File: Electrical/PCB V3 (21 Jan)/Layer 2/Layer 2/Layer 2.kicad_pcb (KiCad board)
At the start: 2 copper layers, 178 x 170 mm, 67 parts, among them Q1 AON6354, Q2 AON6354, Q3 AON6354, Q4 AON6354, SW1 SW_Nidec_CAS-120A1, U2 LM2596S-3.3, U3 VNH5019ATR-E, U4 XT30UPB-M, U5 XT30UPB-M, U6 VNH5019ATR-E, U7 VNH5019ATR-E, U8 VNH5019ATR-E, U9 XT30UPB-M

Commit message: halfway done with motor drivers footprint vias are gay
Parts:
- added L2: L, Connector_PinHeader_2.54mm:PinHeader_1x02_P2.54mm_Vertical_SMD_Pin1Right, F.Cu at (244.8, 61.0)
- added U10: Pinhead1, Connector_PinHeader_2.54mm:PinHeader_1x02_P2.54mm_Vertical_SMD_Pin1Right, F.Cu at (244.8, 68.2)
- added U11: Pinhead 2, Connector_PinHeader_2.54mm:PinHeader_1x02_P2.54mm_Vertical_SMD_Pin1Right, F.Cu at (244.8, 75.3)
- C2, Q1, R1, R2, R3, R4, R5, R6, R7, R8: moved to B.Cu
- U3: footprint layer2v3:IC_VNH5019ATR-E -> layer2v3:fixed -onenew; moved to B.Cu
- U6, U7, U8: footprint layer2v3:IC_VNH5019ATR-E -> layer2v3:fixed -onenew
- moved U9 254.3 mm to (109.4, 73.3)
- moved C2 131.4 mm to (292.3, 165.5), turned to 180 degrees
- moved R3 125.2 mm to (295.1, 151.4)
- moved R1 124.5 mm to (295.1, 144.8)
- moved R4 121.2 mm to (291.1, 147.3), turned to 180 degrees
- moved R2 120.2 mm to (298.8, 144.8), turned to 180 degrees
- moved R5 118.4 mm to (295.0, 149.3), turned to 180 degrees
- moved R7 117.5 mm to (291.1, 151.6), turned to 180 degrees
- moved R6 114.3 mm to (291.1, 144.9), turned to 180 degrees
- moved R8 113.4 mm to (291.0, 149.4), turned to 180 degrees
- moved U3 112.2 mm to (278.5, 150.5), turned to 180 degrees
- moved Q1 67.5 mm to (292.7, 155.8), turned to 90 degrees
- moved SW1 1.79 mm to (376.0, 88.3)
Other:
- outline, holes or cut-outs redrawn

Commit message: yay fixed motor driver do rest mr cos tired djbfj
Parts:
- U3, U6, U7, U8: footprint layer2v3:fixed -onenew -> layer2v3:fixed -onenew-newer

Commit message: cx is annoyingwith 1 drivers
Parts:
- added J1: Conn_01x04, Connector_JST:JST_EH_B4B-EH-A_1x04_P2.50mm_Vertical, B.Cu at (89.1, 76.4)
- added J2: Conn_01x06, Connector_JST:JST_EH_B6B-EH-A_1x06_P2.50mm_Vertical, F.Cu at (91.5, 189.6)
- A1: footprint layer2v3:TEENSY_SHORT -> layer2v3:MODULE_DEV-15583
- C4, Q2, R10, R11, R12, R13, R14, R15, R16, R17, U6: moved to B.Cu
- U10: value Pinhead1 -> XT30UPB-M; footprint Connector_PinHeader_2.54mm:PinHeader_1x02_P2.54mm_Vertical_SMD_Pin1Right -> layer2v3:XT30UPB-M
- U11: value Pinhead 2 -> XT30UPB-M; footprint Connector_PinHeader_2.54mm:PinHeader_1x02_P2.54mm_Vertical_SMD_Pin1Right -> layer2v3:XT30UPB-M
- moved H4 316.3 mm to (27.3, 157.9)
- moved H3 311.9 mm to (27.3, 119.1)
- moved H5 293.3 mm to (78.6, 199.1)
- moved H13 288.4 mm to (86.1, 168.5)
- moved H12 275.0 mm to (84.1, 159.5)
- moved H11 269.4 mm to (84.1, 117.5)
- moved H10 267.2 mm to (86.1, 108.5)
- moved R14 256.7 mm to (115.9, 125.4), turned to 180 degrees
- moved R13 256.3 mm to (116.0, 121.4), turned to 180 degrees
- moved R12 255.5 mm to (118.7, 124.4), turned to 90 degrees
- moved R10 254.8 mm to (119.8, 119.4)
- moved R15 254.1 mm to (115.9, 119.5), turned to 180 degrees
- moved R11 253.9 mm to (120.7, 122.3), turned to 90 degrees
- moved R17 253.7 mm to (115.8, 123.5), turned to 180 degrees
- moved R16 250.5 mm to (120.7, 126.1), turned to -90 degrees
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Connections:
- U3 pad 15: /Motor 2 Out B -> /Motor 1 Out B
- U3 pad 16: /Motor 2 Out B -> /Motor 1 Out B
- U3 pad 21: /Motor 2 Out B -> /Motor 1 Out B
- U3 pad HS3: /Motor 2 Out B -> /Motor 1 Out B
- U4 pad P$1: +5V -> /Motor 1 Out A
- U4 pad P$2: GND -> /Motor 1 Out B
- U5 pad P$1: +3V3 -> /Motor 3 Out A
- U5 pad P$2: GND -> /Motor 3 Out B
- U6 pad 15: /Motor 2 BOut  -> /Motor 2 Out B
- U6 pad 16: /Motor 2 BOut  -> /Motor 2 Out B
- U6 pad 21: /Motor 2 BOut  -> /Motor 2 Out B
- U6 pad HS3: /Motor 2 BOut  -> /Motor 2 Out B
- U8 pad 1: /Motor 4 Motor B -> /Motor 4 Out A
- U8 pad 25: /Motor 4 Motor B -> /Motor 4 Out A
- U8 pad 30: /Motor 4 Motor B -> /Motor 4 Out A
- U8 pad HS2: /Motor 4 Motor B -> /Motor 4 Out A
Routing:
- net /Motor 1 EN A: track 0.00 -> 60.3 mm
- net +3V3: track 0.00 -> 50.3 mm, vias 0 -> 1
- net /Motor 1 EN B: track 0.00 -> 21.0 mm, vias 0 -> 2
- net /Motor 4 Out A: track 0.00 -> 13.3 mm
- net Net-(U3-ENB/DIAGB): track 0.00 -> 8.72 mm
- net Net-(U3-INB): track 0.00 -> 3.10 mm
- net Net-(U3-PWM): track 0.00 -> 2.57 mm
- added copper zone on B.Cu, net +12V
- added copper zone on B.Cu, net +3V3
- added copper zone on B.Cu, net /Motor 1 EN A
- added copper zone on B.Cu, net /Motor 1 Out A
- added copper zone on B.Cu, net /Motor 1 Out B
- added copper zone on B.Cu, net /Motor Driver
- added copper zone on B.Cu, net /PWM Motor 1
- added copper zone on B.Cu, net Net-(C2-Pad1)
- added copper zone on B.Cu, net Net-(Q1-G)
- added copper zone on B.Cu, net Net-(U3-ENA/DIAGA)
- added copper zone on B.Cu, net Net-(U3-INA)

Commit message: motor drivers someone done ish ig this is from yesterday
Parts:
- moved R12 1.91 mm to (118.8, 122.5)
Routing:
- net +3V3: track 50.3 -> 97.7 mm, vias 1 -> 2
- net /Motor Driver: track 0.00 -> 41.0 mm, vias 0 -> 1
- net Net-(U6-INA): track 0.00 -> 2.29 mm
- net /Motor 2 EN A: track 0.00 -> 2.23 mm
- net /Motor 2 EN B: track 0.00 -> 2.16 mm
- net Net-(U6-ENA/DIAGA): track 0.00 -> 2.00 mm
- net Net-(U6-ENB/DIAGB): track 0.00 -> 1.89 mm
- net Net-(U6-PWM): track 0.00 -> 1.89 mm
- added copper zone on B.Cu, net /PWM Motor 2
- added copper zone on B.Cu, net Net-(Q2-G)
- added copper zone on B.Cu, net Net-(U6-INB)

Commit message: last motor driver to be done and jst
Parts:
- removed U9: XT30UPB-M, layer2v3:AMASS_XT60-M
- added J3: XT60-M, layer2v3:AMASS_XT60-M, F.Cu at (109.5, 73.2)
- C6, C8, Q3, Q4, R18, R19, R20, R21, R22, R23, R24, R25, R26, R27, R28, R29, R30, R31, R32, R33, U7, U8: moved to B.Cu
- J2: value Conn_01x06 -> Conn_02x04_Counter_Clockwise; footprint Connector_JST:JST_EH_B6B-EH-A_1x06_P2.50mm_Vertical -> Connector_JST:JST_PHD_B8B-PHDSS_2x04_P2.00mm_Vertical
- moved R30 287.1 mm to (116.1, 176.2), turned to 180 degrees
- moved R29 286.7 mm to (116.1, 172.2), turned to 180 degrees
- moved R28 285.7 mm to (119.9, 174.4)
- moved R32 285.3 mm to (116.2, 178.3), turned to 180 degrees
- moved R31 283.2 mm to (116.1, 170.3), turned to 180 degrees
- moved R33 282.4 mm to (116.1, 174.3), turned to 180 degrees
- moved R27 272.6 mm to (119.9, 178.3)
- moved R22 270.6 mm to (117.7, 154.0), turned to 180 degrees
- moved R21 270.1 mm to (117.7, 150.1), turned to 180 degrees
- moved R26 270.0 mm to (122.8, 175.3), turned to -90 degrees
- moved R24 269.1 mm to (117.7, 156.0), turned to 180 degrees
- moved R20 268.8 mm to (121.4, 152.1)
- moved R19 267.1 mm to (123.0, 148.7), turned to 90 degrees
- moved R23 267.0 mm to (117.9, 148.2), turned to 180 degrees
- moved R25 266.5 mm to (117.6, 152.0), turned to 180 degrees
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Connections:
- A1 pad 10: unconnected-(A1-Pad10) -> /Motor 4 EN A
- A1 pad 11: unconnected-(A1-Pad11) -> /Motor 4 EN B
- A1 pad 12: unconnected-(A1-Pad12) -> /Motor 1 EN A
- A1 pad 13: /Motor 1 EN A -> unconnected-(A1-Pad13)
- A1 pad 14: /Motor 4 EN B -> /TX1
- A1 pad 15: /Motor 4 EN A -> /RX1
- A1 pad 16: /Motor 3 EN B -> /RX2
- A1 pad 17: /Motor 3 EN A -> /TX2
- A1 pad 18: /Motor 2 EN B -> unconnected-(A1-Pad18)
- A1 pad 19: /Motor 2 EN A -> unconnected-(A1-Pad19)
- A1 pad 20: /Motor 1 EN B -> /TX1
- A1 pad 21: unconnected-(A1-Pad21) -> /RX3
- A1 pad 5: unconnected-(A1-Pad5) -> /Motor 1 EN B
- A1 pad 6: unconnected-(A1-Pad6) -> /Motor 2 EN A
- A1 pad 7: unconnected-(A1-Pad7) -> /Motor 2 EN B
- A1 pad 8: unconnected-(A1-Pad8) -> /Motor 3 EN A
- A1 pad 9: unconnected-(A1-Pad9) -> /Motor 3 EN B
- J2 pad 2: /SCL -> /RX1
- J2 pad 3: /SDA -> /TX1
- J2 pad 4: /L3 TX -> /RX2
- J2 pad 5: /L3 RX -> GND
- J2 pad 6: GND -> /TX3
- R26 pad 1: /Motor 4 EN B -> /Motor 4 EN A
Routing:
- net +12V: track 0.00 -> 215.9 mm, vias 0 -> 3
- net /Motor 3 EN A: track 0.00 -> 96.3 mm, vias 0 -> 3
- net /Motor 3 EN B: track 0.00 -> 92.5 mm, vias 0 -> 2
- net /PWM Motor 3: track 0.00 -> 65.4 mm
- net Net-(C4-Pad1): track 0.00 -> 61.5 mm, vias 0 -> 2
- net /Motor Driver: track 41.0 -> 97.7 mm
- net +3V3: track 97.7 -> 147.9 mm
- net Net-(C6-Pad1): track 0.00 -> 37.6 mm
- net Net-(C2-Pad1): track 0.00 -> 16.7 mm, vias 0 -> 2
- net /Motor 4 Out A: track 13.3 -> 0.00 mm
- net /Motor 4 EN A: track 0.00 -> 7.65 mm
- net Net-(U8-INA): track 0.00 -> 3.24 mm
- net Net-(U7-INA): track 0.00 -> 3.08 mm
- net Net-(U7-ENA/DIAGA): track 0.00 -> 2.55 mm
- net Net-(U7-ENB/DIAGB): track 0.00 -> 2.51 mm
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- added copper zone on B.Cu, net /Motor 2 Out A
- added copper zone on B.Cu, net /Motor 2 Out B
- added copper zone on B.Cu, net /Motor 3 Out A
- added copper zone on B.Cu, net /Motor 3 Out B
- added copper zone on B.Cu, net Net-(C4-Pad1)
- added copper zone on B.Cu, net Net-(C6-Pad1)
- added copper zone on B.Cu, net Net-(Q3-G)
- added copper zone on B.Cu, net Net-(Q4-G)
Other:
- board text added: "2-Chairs."

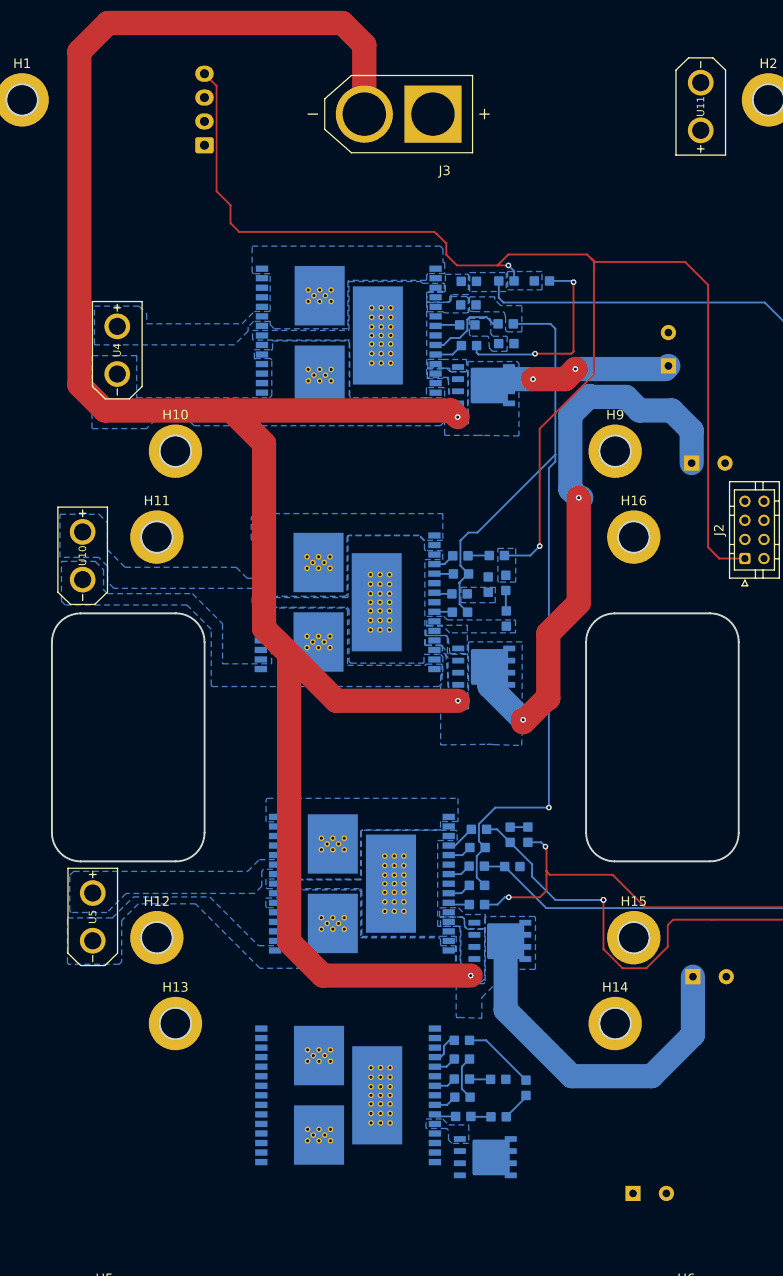
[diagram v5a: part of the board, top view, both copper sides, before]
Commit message: motor drivers r done to be done tmr: diodes footbrint buckies boost capacitors and teensy pwm and motor feedback wiring
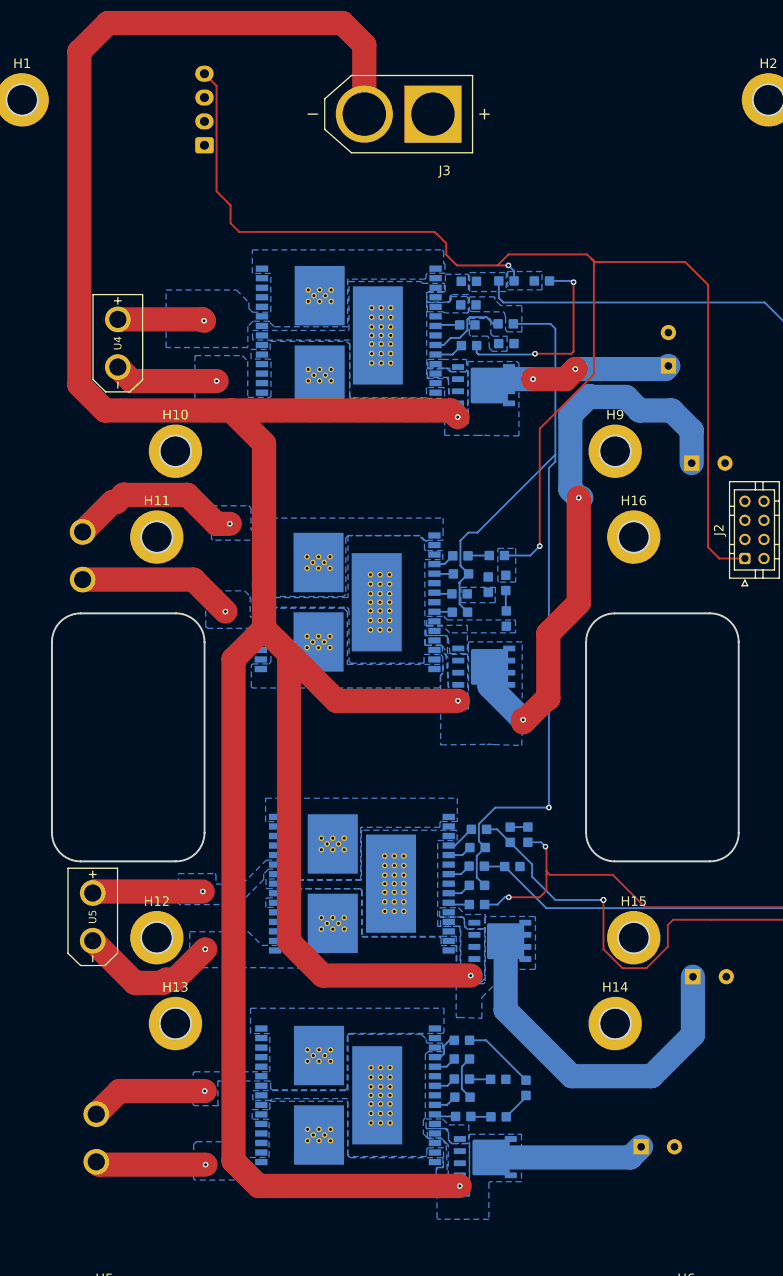
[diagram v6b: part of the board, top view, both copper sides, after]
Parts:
- U10, U11: moved to B.Cu
- moved U11 125.3 mm to (77.8, 180.5), turned to -90 degrees
- moved C8 4.96 mm to (136.6, 181.4)
- moved U4 0.73 mm to (80.0, 97.2)
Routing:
- net +12V: track 215.9 -> 297.8 mm, vias 3 -> 4
- net /Motor 2 Out A: track 0.00 -> 18.3 mm, vias 0 -> 1
- net /Motor 2 Out B: track 0.00 -> 16.4 mm, vias 0 -> 1
- net Net-(C8-Pad1): track 0.00 -> 16.2 mm
- net /Motor 3 Out B: track 0.00 -> 15.1 mm, vias 0 -> 1
- net /Motor 4 Out A: track 0.00 -> 12.4 mm, vias 0 -> 1
- net /Motor 3 Out A: track 0.00 -> 11.6 mm, vias 0 -> 1
- net /Motor 4 Out B: track 0.00 -> 11.6 mm, vias 0 -> 1
- net /Motor 1 Out B: track 0.00 -> 11.0 mm, vias 0 -> 1
- net /Motor 1 Out A: track 0.00 -> 9.10 mm, vias 0 -> 1
- added copper zone on B.Cu, net /Motor 4 Out A
- added copper zone on B.Cu, net /Motor 4 Out B
- added copper zone on B.Cu, net Net-(C8-Pad1)

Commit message: boostie
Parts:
- added C1: 220u, Capacitor_THT:CP_Axial_L10.0mm_D6.0mm_P15.00mm_Horizontal, F.Cu at (245.6, 87.2)
- added C10: 10n, Capacitor_THT:CP_Axial_L10.0mm_D6.0mm_P15.00mm_Horizontal, F.Cu at (260.2, 87.2)
- added C11: 220u, Capacitor_THT:CP_Axial_L10.0mm_D6.0mm_P15.00mm_Horizontal, F.Cu at (260.2, 99.3)
- added C12: 1u, Capacitor_THT:CP_Axial_L10.0mm_D6.0mm_P15.00mm_Horizontal, F.Cu at (131.8, 205.4)
- added C13: 0u1, Capacitor_THT:CP_Axial_L10.0mm_D6.0mm_P15.00mm_Horizontal, F.Cu at (148.7, 186.9)
- added C14: 220uF, Capacitor_THT:CP_Axial_L10.0mm_D6.0mm_P15.00mm_Horizontal, F.Cu at (148.1, 183.5)
- added C3: 220u, Capacitor_THT:CP_Axial_L10.0mm_D6.0mm_P15.00mm_Horizontal, F.Cu at (245.6, 99.3)
- added C5: 0u1, Capacitor_THT:CP_Axial_L10.0mm_D6.0mm_P15.00mm_Horizontal, F.Cu at (108.2, 190.6)
- added C7: 100u, Capacitor_THT:CP_Axial_L10.0mm_D6.0mm_P15.00mm_Horizontal, F.Cu at (104.2, 197.6)
- added C9: 10u, Capacitor_THT:CP_Axial_L10.0mm_D6.0mm_P15.00mm_Horizontal, F.Cu at (245.6, 135.4)
- added D1: SS54, Diode_SMD:D_0201_0603Metric, F.Cu at (282.5, 106.0)
- added D2: SS54, Diode_SMD:D_0201_0603Metric, F.Cu at (282.5, 107.7)
- added D3: SS510, Diode_SMD:D_0201_0603Metric, F.Cu at (132.6, 189.7)
- added L1: 15uH, Inductor_SMD:L_0201_0603Metric, F.Cu at (285.0, 106.0)
- added L3: 68uH, Inductor_SMD:L_APV_APH1040, F.Cu at (115.7, 194.8)
- added R34: 10K, Sen Robo:res0603, F.Cu at (269.7, 106.5)
- added R35: 3K24, Sen Robo:res0603, F.Cu at (269.7, 109.4)
- added R36: 2k94, Sen Robo:res0603, F.Cu at (130.6, 194.4)
- added R37: 57K, Sen Robo:res0603, F.Cu at (132.5, 192.5)
- added R38: 1K5, Sen Robo:res0603, F.Cu at (189.0, 199.5)
- added U1: XT30UPB-M, layer2v3:XT30UPB-M, F.Cu at (137.7, 189.8)
- added U12: TPS5430DDAG4, layer2v3:VREG_TPS79625KTTR, F.Cu at (281.3, 87.3)
- added U9: LM2587S-ADJ, layer2v3:VREG_LM5017MR_NOPB, F.Cu at (125.0, 192.4)
- C2, C4, C6, C8: footprint Sen Robo:CP_Radial_D8.0mm_P3.50mm -> Capacitor_THT:CP_Axial_L10.0mm_D6.0mm_P15.00mm_Horizontal
- moved C8 11.2 mm to (125.5, 182.1)
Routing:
- net +12V: track 297.8 -> 326.1 mm
- net Net-(D3-A): track 0.00 -> 25.3 mm, vias 0 -> 2
- net Net-(C8-Pad1): track 16.2 -> 6.50 mm
- added copper zone on B.Cu, net +24V
- added copper zone on B.Cu, net Net-(D3-A)
- added copper zone on B.Cu, net Net-(U9-COMP)
- added copper zone on B.Cu, net Net-(U9-FB)

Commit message: i think i  added the solenoid boost in this idk
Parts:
- moved R38 55.0 mm to (134.2, 194.3), turned to 0 degrees
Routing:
- added copper zone on B.Cu, net Net-(C12-Pad1)
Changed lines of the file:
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@@
 	(footprint "Sen Robo:res0603"
 		(layer "F.Cu")
-		(at 189.024377 199.51432 90)
+		(at 134.249377 194.31432)
 		(property "Reference" "R38"
-			(at 0 -1.6 90)
+			(at 0 -1.6 360)
 			(layer "F.SilkS")
 			(effects
@@
 		)
 		(property "Value" "1K5"
-			(at 0 1.8 90)
+			(at 0 1.8 0)
 			(unlocked yes)
 			(layer "F.Fab")
@@
 		)
 		(property "Footprint" "Sen Robo:res0603"
-			(at 0 0 90)
+			(at 0 0 360)
 			(layer "F.Fab")
 			(hide yes)
@@
 		)
 		(property "Datasheet" ""
-			(at 0 0 90)
+			(at 0 0 360)
 			(layer "F.Fab")
 			(hide yes)
@@
 		)
 		(property "Description" ""
-			(at 0 0 90)
+			(at 0 0 360)
 			(layer "F.Fab")
 			(hide yes)
@@
 		)
 		(property "LCSC" "C22843"
-			(at 0 0 90)
+			(at 0 0 0)
 			(unlocked yes)
 			(layer "F.Fab")
@@
 		(attr smd)
 		(fp_line
-			(start -1.5 -0.9)
-			(end 1.5 -0.9)
+			(start -1.8 0.6)
+			(end -1.8 -0.6)
 			(stroke
 				(width 0.1)
@@
 		)
 		(fp_line
-			(start 1.8 -0.6)
-			(end 1.8 0.6)
+			(start -1.5 -0.9)
+			(end 1.5 -0.9)
 			(stroke
 				(width 0.1)
@@
 		)
 		(fp_line
-			(start -1.8 0.6)
-			(end -1.8 -0.6)
+			(start -1.5 0.9)
+			(end 1.5 0.9)
 			(stroke
 				(width 0.1)
@@
 		)
 		(fp_line
-			(start -1.5 0.9)
-			(end 1.5 0.9)
+			(start 1.8 -0.6)
+			(end 1.8 0.6)
 			(stroke
 				(width 0.1)
@@
 		)
 		(fp_arc
-			(start 1.5 -0.9)
-			(mid 1.712132 -0.812132)
-			(end 1.8 -0.6)
+			(start -1.8 -0.6)
+			(mid -1.712132 -0.812132)
+			(end -1.5 -0.9)
 			(stroke
 				(width 0.1)
@@
 		)
 		(fp_arc
-			(start -1.8 -0.6)
-			(mid -1.712132 -0.812132)
-			(end -1.5 -0.9)
+			(start -1.5 0.9)
+			(mid -1.712132 0.812132)
+			(end -1.8 0.6)
 			(stroke
 				(width 0.1)
@@
 		)
 		(fp_arc
-			(start 1.8 0.6)
-			(mid 1.712132 0.812132)
-			(end 1.5 0.9)
+			(start 1.5 -0.9)
+			(mid 1.712132 -0.812132)
+			(end 1.8 -0.6)
 			(stroke
 				(width 0.1)
@@
 		)
 		(fp_arc
-			(start -1.5 0.9)
-			(mid -1.712132 0.812132)
-			(end -1.8 0.6)
+			(start 1.8 0.6)
+			(mid 1.712132 0.812132)
+			(end 1.5 0.9)
 			(stroke
 				(width 0.1)
@@
 		)
 		(pad "1" smd roundrect
-			(at -0.8 0 90)
+			(at -0.8 0)
 			(size 1 1)
 			(layers "F.Cu" "F.Paste" "F.Mask")
@@
 		)
 		(pad "2" smd roundrect
-			(at 0.8 0 90)
+			(at 0.8 0)
 			(size 1 1)
 			(layers "F.Cu" "F.Paste" "F.Mask")
@@
 			(pts
 				(xy 150.419377 188.70432) (xy 150.379377 188.74432) (xy 145.479377 188.74432) (xy 145.269377 188.95432)
-				(xy 145.269377 194.24432) (xy 144.059377 195.45432) (xy 132.869377 195.45432) (xy 132.539377 195.12432)
+				(xy 145.269377 193.20432) (xy 145.279377 193.12432) (xy 132.549377 193.12432) (xy 132.539377 193.11432)
 				(xy 132.539377 188.15432) (xy 132.829377 187.86432) (xy 137.359377 187.86432) (xy 137.549377 188.05432)
 				(xy 137.549377 191.64432) (xy 137.739377 191.83432) (xy 142.969377 191.83432) (xy 143.619377 191.18432)
@@
 	)
 	(zone
+		(net 86)
+		(net_name "Net-(C12-Pad1)")
+		(layer "B.Cu")
+		(hatch edge 0.5)
+		(priority 34)
+		(connect_pads yes
+			(clearance 0.2)
+		)
+		(min_thickness 0.25)
+		(filled_areas_thickness no)
+		(fill yes
+			(thermal_gap 0.5)
+			(thermal_bridge_width 0.5)
+			(smoothing chamfer)
+			(radius 0.25)
+		)
+		(polygon
+			(pts
+				(xy 130.679377 207.20432) (xy 130.839377 207.36432) (xy 133.209377 207.36432) (xy 133.209377 196.10432)
+				(xy 132.209377 195.10432) (xy 132.209377 193.73432) (xy 132.159377 193.68432) (xy 130.679377 193.68432)
+			)
+		)
+	)
+	(zone
 		(net 90)
 		(net_name "Net-(U9-COMP)")
@@
 	)
 	(zone
+		(net 91)
+		(net_name "Net-(U9-FB)")
+		(layer "B.Cu")
+		(hatch edge 0.5)
+		(priority 33)
+		(connect_pads yes
+			(clearance 0.2)
+		)
+		(min_thickness 0.25)
+		(filled_areas_thickness no)
+		(fill yes
+			(thermal_gap 0.5)
+			(thermal_bridge_width 0.5)
+			(smoothing chamfer)
+			(radius 0.25)
+		)
+		(polygon
+			(pts
+				(xy 134.219377 195.15432) (xy 132.539377 195.15432) (xy 132.389377 195.00432) (xy 132.389377 193.44432)
+				(xy 126.809377 193.44432) (xy 126.769377 193.48432) (xy 126.759377 193.47432) (xy 126.759377 192.53432)
+				(xy 126.819377 192.47432) (xy 128.449377 192.47432) (xy 129.009377 191.91432) (xy 129.009377 191.76432)
+				(xy 129.029377 191.74432) (xy 132.359377 191.74432) (xy 132.549377 191.93432) (xy 132.549377 193.12432)
+				(xy 132.699377 193.27432) (xy 134.209377 193.27432) (xy 134.219377 193.28432)
+			)
+		)
+	)
+	(zone
 		(net 12)
 		(net_name "+3V3")
@@
 			)
 		)
-	)
-	(zone
-		(net 91)
-		(net_name "Net-(U9-FB)")
-		(layer "B.Cu")
-		(hatch edge 0.5)
-		(priority 33)
-		(connect_pads yes
-			(clearance 0.2)
-		)
-		(min_thickness 0.25)
-		(filled_areas_thickness no)
-		(fill yes
-			(thermal_gap 0.5)
-			(thermal_bridge_width 0.5)
-			(smoothing chamfer)
-			(radius 0.25)
-		)
-		(polygon
-			(pts
-				(xy 126.569377 193.51432) (xy 128.769377 193.51432) (xy 128.959377 193.32432) (xy 132.309377 193.32432)
-				(xy 132.309377 191.77432) (xy 129.099377 191.77432) (xy 128.519377 192.35432) (xy 126.569377 192.35432)
-			)
-		)
